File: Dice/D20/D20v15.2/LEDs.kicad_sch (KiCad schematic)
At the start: 15 parts

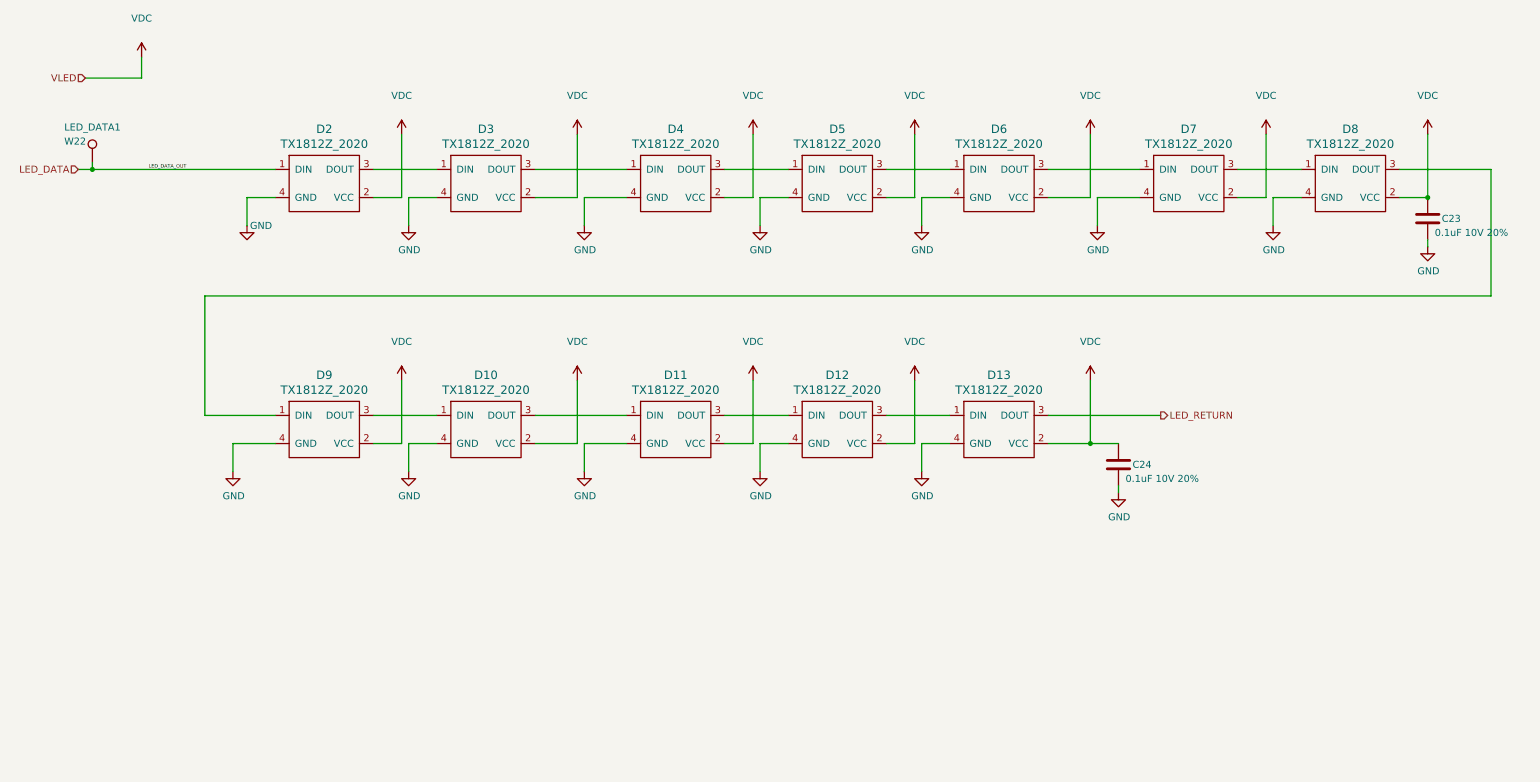
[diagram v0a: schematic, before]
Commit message: New Version of All boards! Better Sticky tape shapes, tweaks to board outline, changed C19 footprint, revert coil pads to through holes. Also updated to Kicad 7.
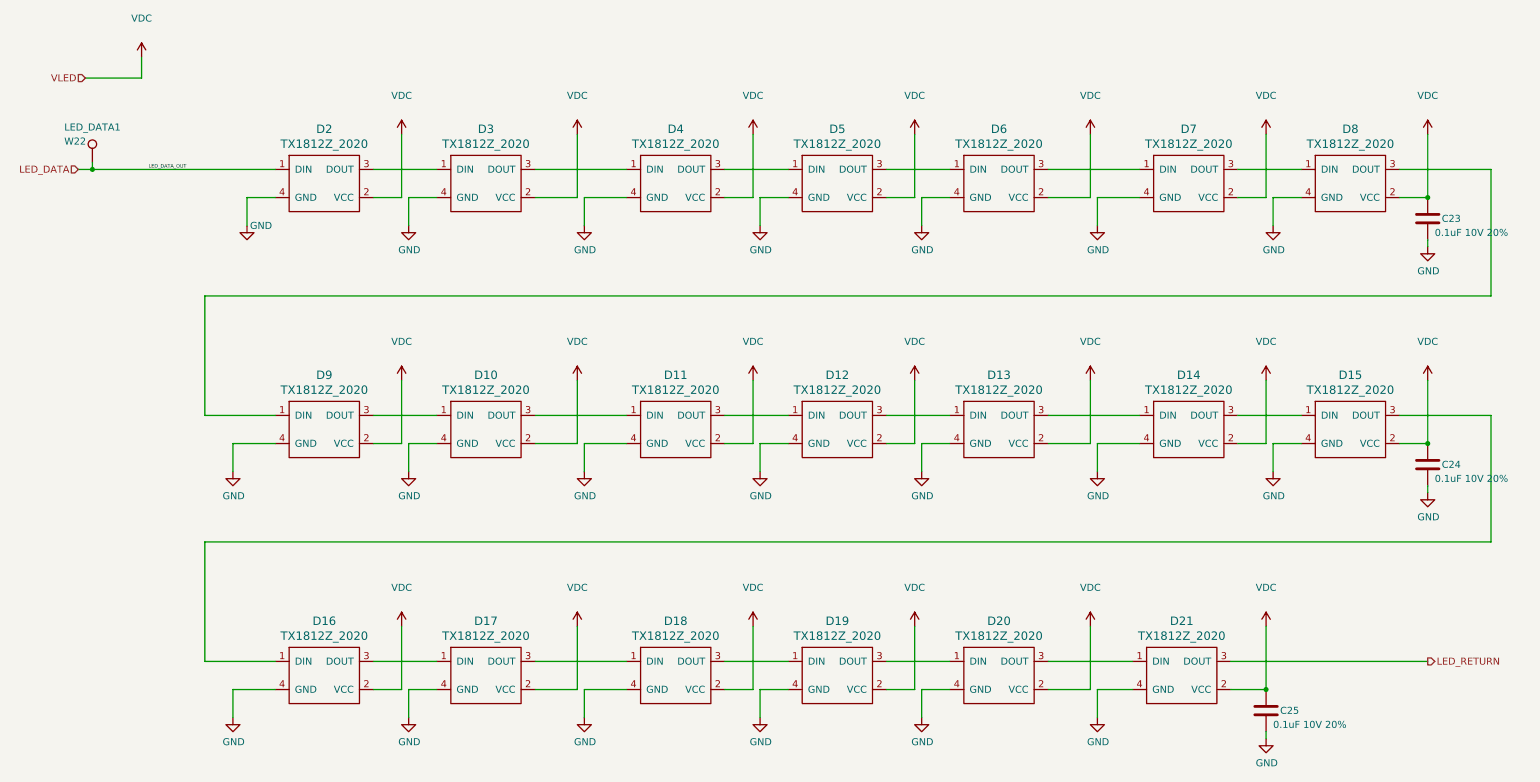
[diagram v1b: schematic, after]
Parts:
- added C25: 0.1uF 10V 20%, Pixels-dice:C_0402_1005Metric, symbol Device:C
- added D14, D15, D16, D17, D18, D19, D20, D21: TX1812Z_2020, Pixels-dice:TX1812Z_2020, symbol Pixels-dice:TX1812Z_2020
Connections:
- net GND: now also C25.2, D14.4 (GND), D15.4 (GND), D16.4 (GND), D17.4 (GND), D18.4 (GND), D19.4 (GND), D20.4 (GND), D21.4 (GND)
- net LED_RETURN: now also D21.3 (DOUT); no longer D13.3 (DOUT)
- net VDC: now also C25.1, D14.2 (VCC), D15.2 (VCC), D16.2 (VCC), D17.2 (VCC), D18.2 (VCC), D19.2 (VCC), D20.2 (VCC), D21.2 (VCC)
- new net: D13.3 (DOUT), D14.1 (DIN)
- new net: D14.3 (DOUT), D15.1 (DIN)
- new net: D15.3 (DOUT), D16.1 (DIN)
- new net: D16.3 (DOUT), D17.1 (DIN)
- new net: D17.3 (DOUT), D18.1 (DIN)
- new net: D18.3 (DOUT), D19.1 (DIN)
- new net: D19.3 (DOUT), D20.1 (DIN)
- new net: D20.3 (DOUT), D21.1 (DIN)
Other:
- title: Pixels D20 Schematic, LEDs -> Pixels D20 Schematic, Main
- moved on the sheet: C24
